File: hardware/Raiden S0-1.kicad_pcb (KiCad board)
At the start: 4 copper layers, 36 x 60 mm, 46 parts, among them J1 Conn_01x15, J2 Conn_01x15, J4 Conn_02x03_Counter_Clockwise, J5 Conn_02x02_Counter_Clockwise, J6 Conn_02x02_Counter_Clockwise, P1 USB_C_Receptacle_USB2.0_14P, SW1 SW_Push, SW2 SW_Push, U1 ESP32-S3FN8, U2 AZ1117C-3.3, Y1 32.768kHz, Y2 40MHz

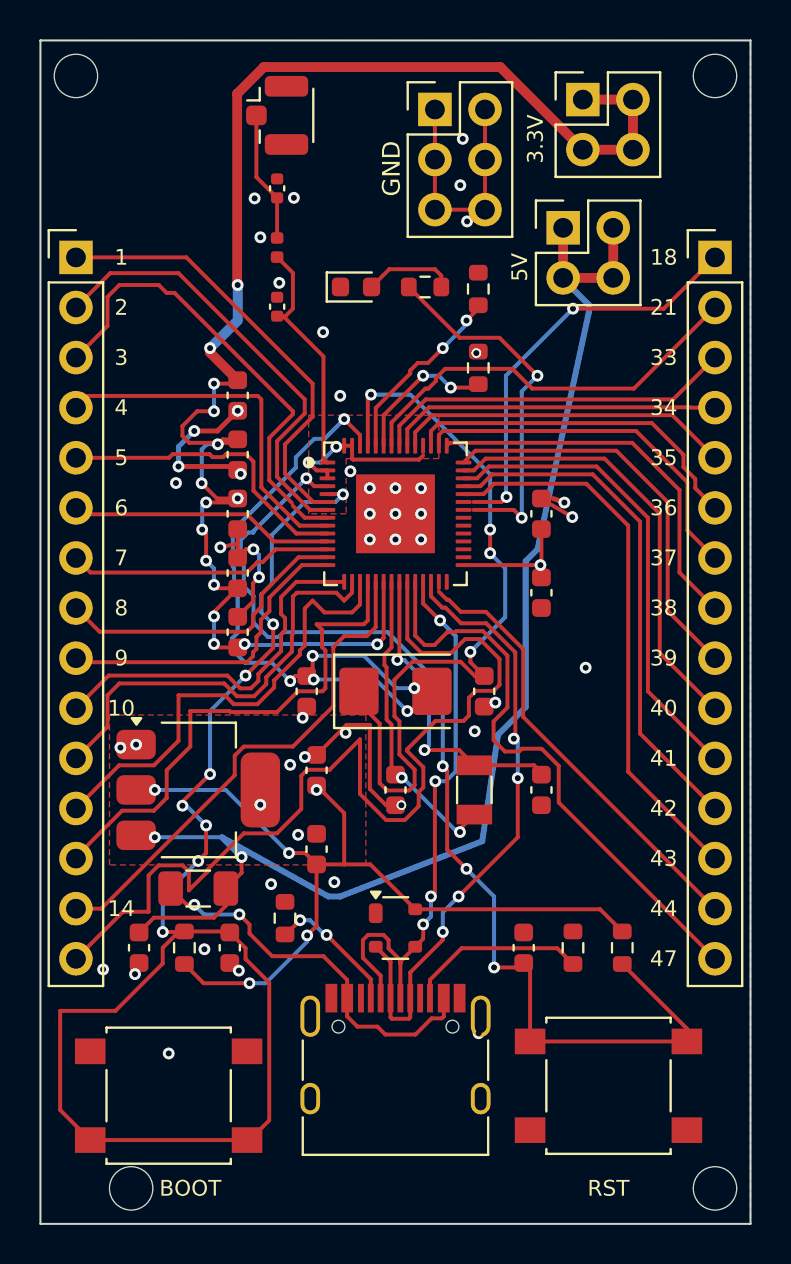
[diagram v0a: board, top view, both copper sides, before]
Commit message: Rev A2: move USB-C to the board edge, plus review fixes
A build-grant reviewer pointed out from the renders that the USB-C port
does not reach the edge of the board. Measured: the connector body ended
3.75 mm short of the edge, so a cable would have hit the PCB before the
plug seated. The board could not have been used.

- USB-C moved down so its face lands on the board edge. The VBUS and D+
  pads are bridged underneath the connector for reversibility; that
  fan-out had to travel with it. Moving the connector alone shorted CC2
  to VBUS, which DRC caught.
- Corners rounded at R = 1.8 mm, equal to the mounting-hole inset, so the
  arcs are concentric with the holes and the web between hole and edge
  stays 0.70 mm.
- The fourth mounting hole was 4.6 mm in while the others were 1.8 mm,
  because the BOOT button sat in that corner. Button moved up 0.3 mm and
  the hole aligned with the rest.
- Front silkscreen: lightning bolt and RAIDEN wordmark, in the one 12x4 mm
  gap a free-space scan found.

ERC 0 errors, DRC 0 errors, 0 unconnected items, 0 parity issues.
Gerbers, drill, placement files and all renders regenerated from the
revised board. Schematic and BOM are unchanged.
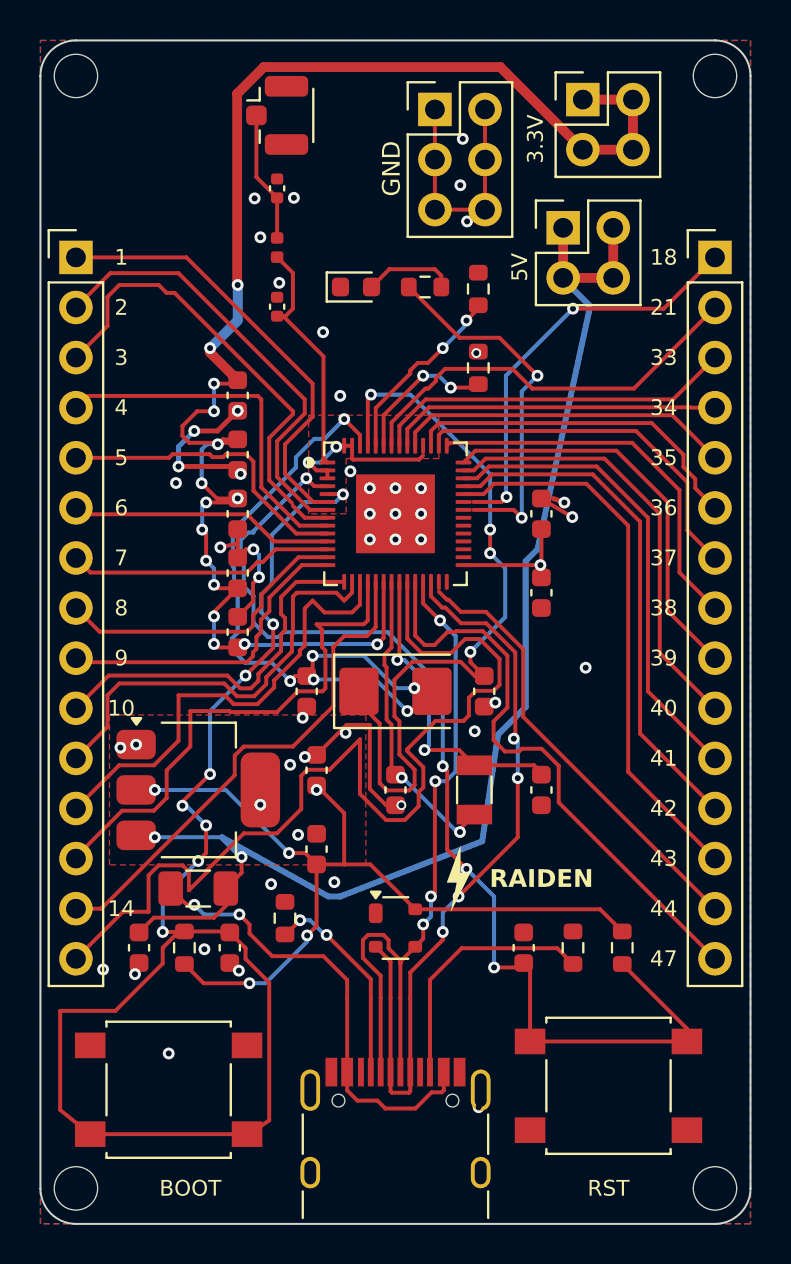
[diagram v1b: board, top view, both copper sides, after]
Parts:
- moved P1 3.75 mm to (118.0, 156.3)
- moved H3 2.80 mm to (101.8, 158.2)
- moved SW1 0.30 mm to (106.5, 153.2)
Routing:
- net Net-(D1-I/O2): track 29.5 -> 37.0 mm
- net Net-(D1-I/O1): track 32.0 -> 39.5 mm
- net Net-(F1-Pad1): track 19.6 -> 23.3 mm
- net Net-(P1-CC2): track 9.17 -> 12.9 mm
- net Net-(P1-CC1): track 6.85 -> 10.6 mm
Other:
- outline, holes or cut-outs redrawn
- board text added: "RAIDEN"
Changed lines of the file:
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@@
 	(footprint "Button_Switch_SMD:SW_SPST_B3S-1000"
 		(layer "F.Cu")
-		(at 106.5 153.5)
+		(at 106.5 153.2)
 		(descr "Surface Mount Tactile Switch for High-Density Packaging")
 		(tags "Tactile Switch")
@@
 	(footprint "MountingHole:MountingHole_2.2mm_M2"
 		(layer "F.Cu")
-		(at 104.6 158.2)
+		(at 101.8 158.2)
 		(property "Reference" "H3"
 			(at 0 -2.2 0)
@@
 	(footprint "Connector_USB:USB_C_Receptacle_HRO_TYPE-C-31-M-12"
 		(layer "F.Cu")
-		(at 118 152.6)
+		(at 118 156.35)
 		(descr "USB Type-C receptacle for USB 2.0 and PD, http://www.krhro.com/uploads/soft/180320/1-1P320120243.pdf")
 		(tags "usb usb-c 2.0 pd")
@@
 		(fp_line
 			(start -4.7 2)
-			(end -4.7 3.9)
-			(stroke
-				(width 0.12)
-				(type solid)
-			)
-			(layer "F.SilkS")
-		)
-		(fp_line
-			(start -4.7 3.9)
-			(end 4.7 3.9)
+			(end -4.7 3.35)
 			(stroke
 				(width 0.12)
@@
 		(fp_line
 			(start 4.7 2)
-			(end 4.7 3.9)
+			(end 4.7 3.35)
 			(stroke
 				(width 0.12)
@@
 		(layer "B.SilkS")
 	)
-	(gr_rect
-		(start 100 100)
-		(end 136 160)
+	(gr_arc
+		(start 100 101.8)
+		(mid 100.5272 100.5272)
+		(end 101.8 100)
+		(stroke
+			(width 0.1)
+			(type default)
+		)
+		(layer "Edge.Cuts")
+	)
+	(gr_line
+		(start 134.2 160)
+		(end 101.8 160)
+		(stroke
+			(width 0.1)
+			(type default)
+		)
+		(layer "Edge.Cuts")
+	)
+	(gr_line
+		(start 136 101.8)
+		(end 136 158.2)
+		(stroke
+			(width 0.1)
+			(type default)
+		)
+		(layer "Edge.Cuts")
+	)
+	(gr_line
+		(start 101.8 100)
+		(end 134.2 100)
+		(stroke
+			(width 0.1)
+			(type default)
+		)
+		(layer "Edge.Cuts")
+	)
+	(gr_arc
+		(start 134.2 100)
+		(mid 135.4728 100.5272)
+		(end 136 101.8)
+		(stroke
+			(width 0.1)
+			(type default)
+		)
+		(layer "Edge.Cuts")
+	)
+	(gr_arc
+		(start 101.8 160)
+		(mid 100.5272 159.4728)
+		(end 100 158.2)
+		(stroke
+			(width 0.1)
+			(type default)
+		)
+		(layer "Edge.Cuts")
+	)
+	(gr_line
+		(start 100 158.2)
+		(end 100 101.8)
+		(stroke
+			(width 0.1)
+			(type default)
+		)
+		(layer "Edge.Cuts")
+	)
+	(gr_arc
+		(start 136 158.2)
+		(mid 135.4728 159.4728)
+		(end 134.2 160)
 		(stroke
 			(width 0.1)
 			(type default)
 		)
-		(fill no)
 		(layer "Edge.Cuts")
 	)
@@
 	)
 	(via
-		(at 122.215 150.333)
+		(at 122.215 154.083)
 		(size 0.6)
 		(drill 0.3)
@@
 	)
 	(segment
-		(start 117.818 149.6)
-		(end 117.75 149.532)
+		(start 117.818 153.35)
+		(end 117.75 153.282)
+		(width 0.2)
+		(layer "F.Cu")
+		(net 36)
+	)
+	(segment
+		(start 118.75 148.555)
+		(end 118.75 152.305)
 		(width 0.2)
 		(layer "F.Cu")
@@
 	)
 	(segment
+		(start 117.75 148.555)
+		(end 117.75 152.305)
+		(width 0.2)
+		(layer "F.Cu")
+		(net 36)
+	)
+	(segment
 		(start 119.8 127.45)
 		(end 119.8 128.180674)
@@
 	)
 	(segment
-		(start 117.75 149.532)
-		(end 117.75 148.555)
+		(start 117.75 153.282)
+		(end 117.75 152.305)
 		(width 0.2)
 		(layer "F.Cu")
@@
 	)
 	(segment
-		(start 118.75 149.532)
-		(end 118.682 149.6)
+		(start 118.75 153.282)
+		(end 118.682 153.35)
 		(width 0.2)
 		(layer "F.Cu")
@@
 	)
 	(segment
-		(start 118.75 148.555)
-		(end 118.75 149.532)
+		(start 118.75 152.305)
+		(end 118.75 153.282)
 		(width 0.2)
 		(layer "F.Cu")
@@
 	)
 	(segment
-		(start 118.682 149.6)
-		(end 117.818 149.6)
+		(start 118.682 153.35)
+		(end 117.818 153.35)
 		(width 0.2)
 		(layer "F.Cu")
@@
 	)
 	(segment
+		(start 118.25 148.555)
+		(end 118.25 152.305)
+		(width 0.2)
+		(layer "F.Cu")
+		(net 37)
+	)
+	(segment
+		(start 117.25 148.555)
+		(end 117.25 152.305)
+		(width 0.2)
+		(layer "F.Cu")
+		(net 37)
+	)
+	(segment
 		(start 118.25 146.8)
 		(end 118.25 146.7)
@@
 	)
 	(segment
-		(start 115.55 149.48)
-		(end 115.55 148.555)
+		(start 115.55 153.23)
+		(end 115.55 152.305)
 		(width 0.2)
 		(layer "F.Cu")
@@
 	)
 	(segment
-		(start 120.45 149.48)
-		(end 120.349 149.581)
+		(start 120.45 153.23)
+		(end 120.349 153.331)
 		(width 0.2)
 		(layer "F.Cu")
@@
 	)
 	(segment
-		(start 119.01337 150.4)
-		(end 117.486628 150.399999)
+		(start 119.01337 154.15)
+		(end 117.486628 154.15)
 		(width 0.2)
 		(layer "F.Cu")
@@
 	)
 	(segment
-		(start 117.486628 150.399999)
-		(end 117.08663 150)
+		(start 117.486628 154.15)
+		(end 117.08663 153.75)
 		(width 0.2)
 		(layer "F.Cu")
@@
 	(segment
 		(start 115.55 148.555)
+		(end 115.55 152.305)
+		(width 0.2)
+		(layer "F.Cu")
+		(net 39)
+	)
+	(segment
+		(start 115.55 148.555)
 		(end 115.55 147.63)
 		(width 0.2)
@@
 	)
 	(segment
-		(start 120.349 149.581)
-		(end 119.83237 149.581)
+		(start 120.349 153.331)
+		(end 119.83237 153.331)
 		(width 0.2)
 		(layer "F.Cu")
@@
 	)
 	(segment
-		(start 117.08663 150)
-		(end 116.07 150)
+		(start 117.08663 153.75)
+		(end 116.07 153.75)
 		(width 0.2)
 		(layer "F.Cu")
@@
 	)
 	(segment
-		(start 119.83237 149.581)
-		(end 119.01337 150.4)
+		(start 119.83237 153.331)
+		(end 119.01337 154.15)
 		(width 0.2)
 		(layer "F.Cu")
@@
 	)
 	(segment
-		(start 120.45 148.555)
-		(end 120.45 149.48)
+		(start 120.45 152.305)
+		(end 120.45 153.23)
 		(width 0.2)
 		(layer "F.Cu")
@@
 	)
 	(segment
-		(start 116.07 150)
-		(end 115.55 149.48)
+		(start 116.07 153.75)
+		(end 115.55 153.23)
 		(width 0.2)
 		(layer "F.Cu")
@@
 		(net 40)
 	)
+	(segment
+		(start 116.75 148.555)
+		(end 116.75 152.305)
+		(width 0.2)
+		(layer "F.Cu")
+		(net 40)
+	)
 	(via
 		(at 114.509918 145.3504)
@@
 	)
 	(segment
+		(start 119.75 148.555)
+		(end 119.75 152.305)
+		(width 0.2)
+		(layer "F.Cu")
+		(net 41)
+	)
+	(segment
 		(start 127 146.825)
 		(end 126.199 146.024)
@@
 	)
 	(segment
-		(start 102.525 155.75)
+		(start 102.525 155.45)
 		(end 101 154.225)
 		(width 0.2)
@@
 	)
 	(segment
-		(start 110.475 155.75)
-		(end 110.6 155.75)
+		(start 110.475 155.45)
+		(end 110.6 155.45)
 		(width 0.2)
 		(layer "F.Cu")
@@
 	)
 	(segment
-		(start 110.475 155.75)
-		(end 102.525 155.75)
+		(start 110.475 155.45)
+		(end 102.525 155.45)
 		(width 0.2)
 		(layer "F.Cu")
@@
 	)
 	(segment
-		(start 110.6 155.75)
+		(start 110.6 155.45)
 		(end 111.6 154.75)
 		(width 0.2)
@@
 	)
 	(embedded_fonts no)
+	(gr_poly
+		(pts
+			(xy 121.3000 140.8000)
+			(xy 120.6000 142.7000)
+			(xy 121.1000 142.7000)
+			(xy 120.8000 144.2000)
+			(xy 121.8000 142.2000)
+			(xy 121.3000 142.2000)
+		)
+		(stroke
+			(width 0)
+			(type solid)
+		)
+		(fill yes)
+		(layer "F.SilkS")
+	)
+	(gr_text "RAIDEN"
+		(at 125.4 142.5 0)
+		(layer "F.SilkS")
+		(effects
+			(font
+				(size 0.9 0.9)
+				(thickness 0.14)
+				(bold yes)
+			)
+		)
+	)
 )
